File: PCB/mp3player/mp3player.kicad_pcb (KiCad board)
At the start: 2 copper layers, 60 x 102 mm, 70 parts, among them J1 AudioJack3, J2 Battery, J3 USB_C, J4 Micro_SD_Card, J5 TFT SPI, SW1 Play, SW10 Power_sw, SW11 Next, SW12 Prev, SW2 Trk Prev, SW3 Trk Next, SW4 Mode Prev, SW5 Mode Next, SW6 Eq, SW7 Power, SW8 RESET, SW9 BOOT, U1 ESP32-S3-WROOM-1, U2 ES8388, U3 AP2112K-3.3, U4 MCP73831-2-OT, U5 USBLC6-2SC6

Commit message: started on placement
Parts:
- moved U2 132.5 mm to (220.1, 86.3)
- moved J1 102.5 mm to (191.0, 102.5), turned to 90 degrees
- moved SW10 101.3 mm to (133.6, 120.5)
- moved SW11 100.0 mm to (211.4, 150.0)
- moved SW12 95.6 mm to (191.6, 150.0)
- moved J5 94.0 mm to (189.0, 81.0)
- moved U1 93.2 mm to (234.0, 90.5)
- moved SW3 91.8 mm to (213.0, 126.5)
- moved SW5 90.9 mm to (201.0, 114.5)
- moved SW4 90.8 mm to (201.0, 138.5)
- moved SW1 90.7 mm to (201.0, 126.5)
- moved SW2 90.0 mm to (189.0, 126.5)
- moved SW7 89.4 mm to (224.7, 121.2), turned to 90 degrees
- moved SW9 77.9 mm to (155.2, 116.2)
- moved J3 24.6 mm to (107.5, 30.0)
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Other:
- board size 60 x 102 mm -> 60 x 85.5 mm

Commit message: cont.
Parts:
- J5: footprint Connector_PinSocket_2.00mm:PinSocket_1x08_P2.00mm_Vertical -> Connector_JST:JST_GH_SM08B-GHS-TB_1x08-1MP_P1.25mm_Horizontal
- moved J5 28.8 mm to (214.5, 94.5), turned to 180 degrees
- moved J1 20.1 mm to (189.5, 82.5), turned to 0 degrees
- moved U2 19.2 mm to (221.5, 105.5)

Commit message: worked on pcb
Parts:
- C1, C10, C11, C12, C13, C14, C15, C16, C17, C18, C19, C2, C20, C21, C22, C3, C4, C5, C6, C7, C8, C9, J1, R1, R10, R11, R12, R13, R14, R15, R16, R17, R18, R19, R2, R20, R21, R22, R23, R24, R3, R4, R5, R6, R7, R8, R9, U1, U2: moved to B.Cu
- J2: footprint Connector_PinSocket_2.00mm:PinSocket_1x02_P2.00mm_Vertical -> Connector_PinSocket_2.00mm:PinSocket_1x02_P2.00mm_Horizontal; moved to B.Cu
- SW8: footprint Button_Switch_SMD:SW_Push_1P1T_NO_Vertical_Wuerth_434133025816 -> Button_Switch_SMD:SW_SPST_PTS810
- SW9: footprint Button_Switch_THT:SW_PUSH_6mm_H4.3mm -> Button_Switch_SMD:SW_SPST_PTS810
- moved C9 174.7 mm to (239.0, 121.8), turned to 180 degrees
- moved C10 174.3 mm to (239.0, 129.0), turned to 180 degrees
- moved J3 172.2 mm to (240.0, 140.0), turned to 90 degrees
- moved RV1 162.5 mm to (237.5, 152.5), turned to 90 degrees
- moved J4 130.4 mm to (190.9, 104.5), turned to 90 degrees
- moved J2 128.3 mm to (187.2, 158.0), turned to 180 degrees
- moved SW8 118.9 mm to (194.5, 87.0), turned to 90 degrees
- moved SW10 62.3 mm to (190.1, 94.2)
- moved C1 59.6 mm to (139.2, 85.0), turned to 180 degrees
- moved C11 59.6 mm to (143.5, 99.8), turned to 180 degrees
- moved C12 59.6 mm to (143.5, 102.3), turned to 180 degrees
- moved C13 59.6 mm to (143.5, 104.8), turned to 180 degrees
- moved C15 59.6 mm to (139.2, 91.0), turned to 180 degrees
- moved C17 59.6 mm to (139.2, 94.0), turned to 180 degrees
- moved C18 59.6 mm to (139.2, 97.0), turned to 180 degrees
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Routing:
- net /BTN_PLAY: track 0.00 -> 43.7 mm, vias 0 -> 3
- net /BTN_TRK_NEXT: track 0.00 -> 42.6 mm, vias 0 -> 1
- net /BTN_EQ: track 0.00 -> 34.1 mm, vias 0 -> 1
- net /TFT_BL: track 0.00 -> 29.2 mm, vias 0 -> 1
- net /TFT_CS: track 0.00 -> 29.0 mm, vias 0 -> 1
- net /TFT_MOSI: track 0.00 -> 24.0 mm, vias 0 -> 1
- net /ROUT1: track 0.00 -> 22.8 mm
- net /TFT_RST: track 0.00 -> 22.6 mm, vias 0 -> 1
- net /TFT_DC: track 0.00 -> 22.4 mm, vias 0 -> 1
- net /TFT_SCK: track 0.00 -> 21.9 mm, vias 0 -> 1
- net /EN: track 0.00 -> 19.6 mm
- net /BTN_POWER: track 0.00 -> 19.5 mm
- net +3V3: track 0.00 -> 19.2 mm
- net /12C_SDA: track 0.00 -> 17.9 mm, vias 0 -> 2
- net /12C_SCL: track 0.00 -> 17.6 mm, vias 0 -> 2
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
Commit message: keys are connected
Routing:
- net /PREV: track 6.50 -> 93.0 mm, vias 0 -> 4
- net /NEXT: track 6.50 -> 72.2 mm, vias 0 -> 2
- net /BTN_TRK_PREV: track 6.50 -> 56.3 mm, vias 0 -> 3
- net /BTN_MODE_PREV: track 6.50 -> 49.9 mm, vias 0 -> 3
- net /BTN_MODE_NEXT: track 6.50 -> 37.4 mm, vias 0 -> 1

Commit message: cont.
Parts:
- U5: moved to B.Cu
- moved U5 166.1 mm to (231.2, 141.2), turned to 180 degrees
- moved U4 142.0 mm to (187.5, 154.2)
- moved D1 122.9 mm to (198.8, 79.2), turned to 90 degrees
- moved R21 36.6 mm to (192.0, 100.0)
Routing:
- net /SLIDE_POT: track 0.00 -> 68.7 mm, vias 0 -> 3
- net /IO0: track 0.00 -> 40.8 mm, vias 0 -> 1
- net /EN: track 19.6 -> 51.5 mm, vias 0 -> 1
- net /USB_DM: track 0.00 -> 9.56 mm, vias 0 -> 1
- net /USB_DP: track 0.00 -> 6.69 mm, vias 0 -> 1

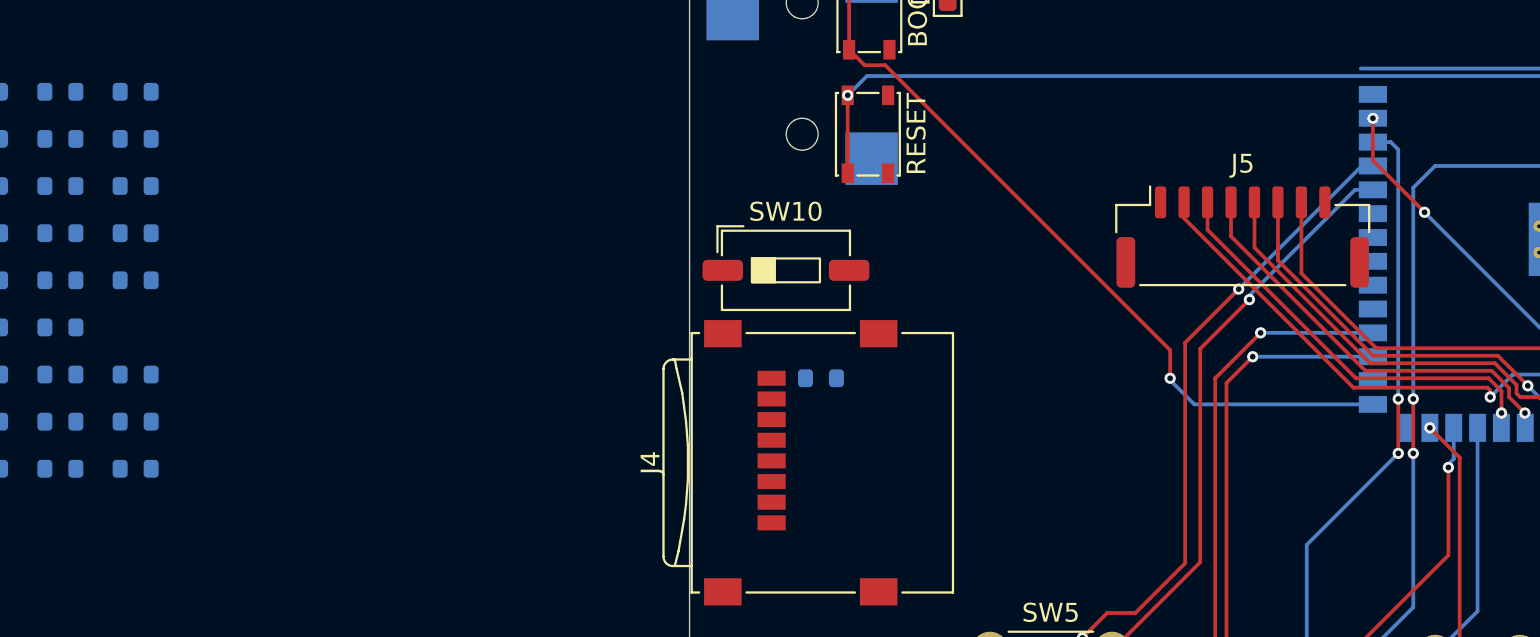
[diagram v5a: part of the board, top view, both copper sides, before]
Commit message: sd pullups done
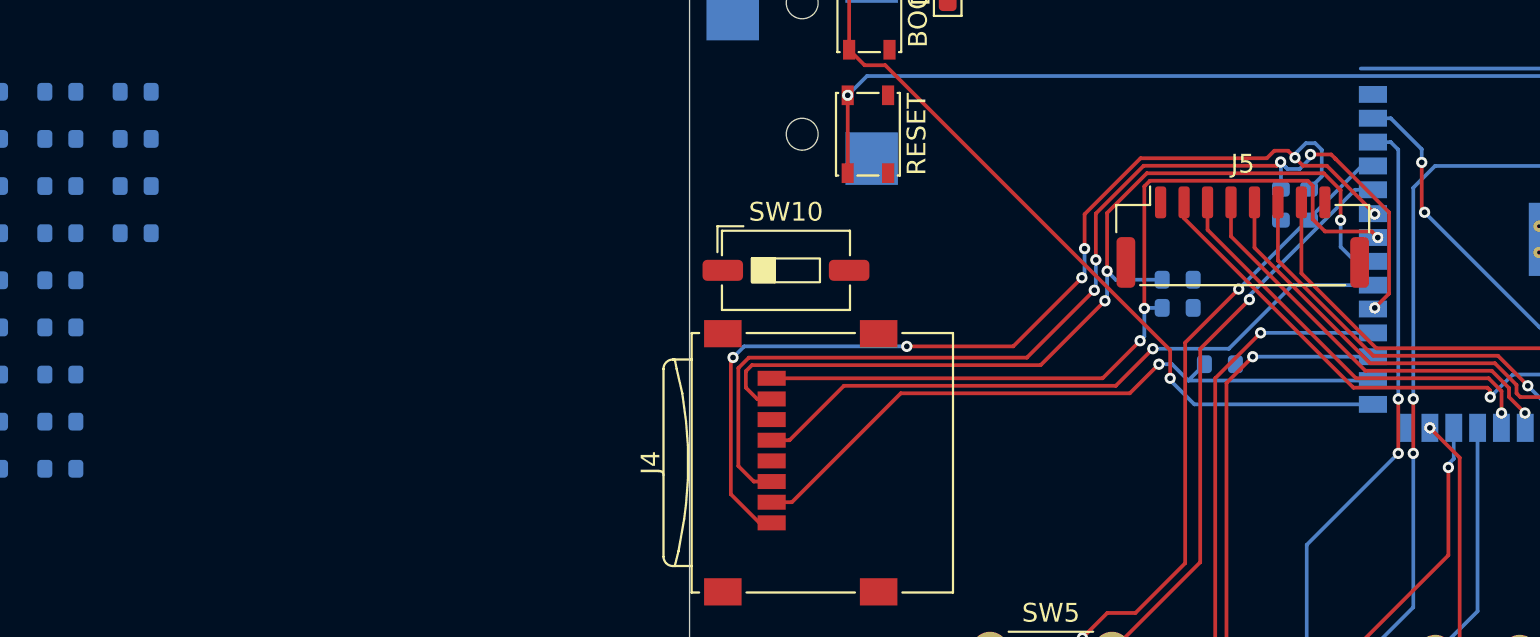
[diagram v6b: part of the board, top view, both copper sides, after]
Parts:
- moved R22 63.2 mm to (218.0, 90.8), turned to 90 degrees
- moved R24 62.6 mm to (216.5, 90.8), turned to 90 degrees
- moved R23 57.8 mm to (213.2, 99.2)
- moved R20 55.5 mm to (211.0, 94.8)
- moved R21 19.4 mm to (211.0, 96.2)
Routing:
- net /SD_CMD: track 0.00 -> 57.8 mm, vias 0 -> 5
- net /SD_D2: track 0.00 -> 56.7 mm, vias 0 -> 6
- net /SD_D0: track 0.00 -> 49.8 mm, vias 0 -> 3
- net /SD_D1: track 0.00 -> 44.9 mm, vias 0 -> 3
- net /SD_D3: track 0.00 -> 36.7 mm, vias 0 -> 1
- net /SD_CLK: track 0.00 -> 35.4 mm, vias 0 -> 1
- net /SLIDE_POT: track 68.7 -> 69.3 mm

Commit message: cont.
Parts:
- R14, R15: value R -> 100k
- R2, R5, R6: moved to F.Cu
- moved R18 99.1 mm to (240.5, 140.8), turned to 0 degrees
- moved R19 97.0 mm to (240.5, 139.0), turned to 0 degrees
- moved R9 93.2 mm to (240.5, 117.2), turned to 0 degrees
- moved R8 90.9 mm to (237.2, 117.2)
- moved R2 86.9 mm to (234.0, 86.2), turned to 90 degrees
- moved U3 83.1 mm to (137.0, 115.5)
- moved R1 81.3 mm to (224.7, 117.8), turned to 90 degrees
- moved R14 63.5 mm to (187.2, 154.8), turned to -90 degrees
- moved R15 62.5 mm to (189.0, 154.8), turned to 90 degrees
- moved R6 44.4 mm to (187.2, 85.0), turned to 0 degrees
- moved R5 42.8 mm to (187.2, 86.5), turned to 0 degrees
- moved U4 13.5 mm to (174.5, 157.8)
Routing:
- net /HP_L: track 0.00 -> 7.37 mm, vias 0 -> 1
- net +3V3: track 19.2 -> 24.8 mm
- net /CC1: track 0.00 -> 5.46 mm, vias 0 -> 1
- net /HP_R: track 0.00 -> 4.42 mm, vias 0 -> 1
- net /12C_SDA: track 17.9 -> 21.7 mm
- net VBAT: track 0.00 -> 2.43 mm
- net /BTN_POWER: track 19.5 -> 21.7 mm
- net /EN: track 51.5 -> 53.3 mm, vias 1 -> 2
- net /VBAT_SENSE: track 0.00 -> 1.75 mm
- net /CC2: track 0.00 -> 1.62 mm, vias 0 -> 1
- net AU_GND: track 6.41 -> 7.91 mm
- net /USB_DM: track 9.56 -> 8.19 mm
- net /12C_SCL: track 17.6 -> 18.6 mm

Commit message: cont.
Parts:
- R14, R15: value 100k -> R
- R16, R17: moved to F.Cu
- moved R17 69.4 mm to (189.0, 148.0), turned to 90 degrees
- moved R16 45.4 mm to (200.5, 79.0), turned to 90 degrees
- moved C14 18.9 mm to (149.7, 103.5)
- moved U4 14.9 mm to (187.9, 151.3)
- moved D1 0.21 mm to (198.8, 79.0)
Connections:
- U4 pad 1: /CHG_PROG -> /CHG_STAT
- U4 pad 3: unconnected-(U4-V_{BAT}-Pad3) -> VBAT
- U4 pad 5: /CHG_STAT -> /CHG_PROG
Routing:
- net /CHG_STAT: track 0.00 -> 78.7 mm, vias 0 -> 2
- net VBAT: track 2.43 -> 69.5 mm, vias 0 -> 2
- net VBUS: track 0.00 -> 45.7 mm, vias 0 -> 1
- net GND: track 0.42 -> 5.87 mm
- net Net-(D1-A): track 0.00 -> 1.75 mm
- net /CHG_PROG: track 0.00 -> 1.54 mm
